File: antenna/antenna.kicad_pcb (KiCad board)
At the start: 2 copper layers, 50 x 43.3 mm, 17 parts, among them J1 Conn_01x05_Pin, J2 Conn_01x05_Pin, J3 Conn_01x05_Pin, J5 USB_C_Receptacle, U1 ESP32-C3-WROOM-02, U2 AMS1117-3.3

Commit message: great success!
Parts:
- removed JP1: SolderJumper_2_Open, Jumper:SolderJumper-2_P1.3mm_Open_RoundedPad1.0x1.5mm
- added C6: 4u7F, Capacitor_SMD:C_0805_2012Metric_Pad1.18x1.45mm_HandSolder, B.Cu at (138.8, 86.8)
- added R1: 10k, Resistor_SMD:R_0805_2012Metric_Pad1.20x1.40mm_HandSolder, B.Cu at (136.2, 86.8)
- added R2: 10k, Resistor_SMD:R_0805_2012Metric_Pad1.20x1.40mm_HandSolder, B.Cu at (138.8, 82.5)
- added SW1: SW_Push, 0_NRD_footprints:SW_PUSH-12mm_Wuerth-430456085736, B.Cu at (147.5, 64.8)
- added SW2: SW_Push, Button_Switch_SMD:SW_Tactile_SPST_NO_Straight_CK_PTS636Sx25SMTRLFS, B.Cu at (164.5, 91.0)
- C1: value C -> 4u7F
- C2: value 100nF -> 4u7F
- moved C4 10.2 mm to (133.0, 82.2), turned to 60 degrees
- moved C5 7.60 mm to (136.2, 82.5), turned to 90 degrees
- moved U2 4.51 mm to (133.2, 87.0), turned to -90 degrees
- moved C3 2.75 mm to (138.8, 91.0)
- moved C2 1.85 mm to (136.2, 91.0)
- moved D1 1.02 mm to (151.0, 86.5)
- moved U1 0.98 mm to (150.0, 86.2)
- moved C1 0.75 mm to (145.5, 86.0)
- moved J1 0.73 mm to (155.8, 91.2)
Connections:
- J2 pad 3: Net-(J2-Pin_3) -> unconnected-(J2-Pin_3-Pad3)
- U1 pad 16: unconnected-(U1-IO2-Pad16) -> Net-(D1-DIN)
- U1 pad 18: Net-(D1-DIN) -> Net-(U1-IO0)
- U1 pad 2: unconnected-(U1-EN-Pad2) -> Net-(U1-EN)
- U1 pad 7: unconnected-(U1-IO8-Pad7) -> Net-(U1-IO8)
- U1 pad 8: unconnected-(U1-IO9-Pad8) -> Net-(U1-IO9)
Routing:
- net GND: track 28.2 -> 178.2 mm, vias 5 -> 4
- net +5V: track 39.1 -> 154.0 mm, vias 10 -> 9
- net Net-(U1-IO9): track 0.00 -> 25.6 mm
- net Net-(U1-3V3): track 6.43 -> 23.3 mm, vias 0 -> 2
- net Net-(J2-Pin_3): track 10.5 -> 0.00 mm
- net Net-(D5-DOUT): track 14.1 -> 4.26 mm
- net Net-(U1-EN): track 0.00 -> 8.76 mm
- net /D-: track 9.54 -> 5.89 mm
- net Net-(U1-IO8): track 0.00 -> 3.22 mm
- net Net-(D1-DOUT): track 22.2 -> 19.7 mm
- net Net-(U1-IO0): track 0.00 -> 2.39 mm
- net Net-(D2-DOUT): track 13.9 -> 15.5 mm
- net Net-(D1-DIN): track 15.6 -> 16.5 mm, vias 0 -> 1
- net /D+: track 12.3 -> 11.6 mm
- removed copper zone on B.Cu, net +5V
- removed copper zone on F.Cu, net +5V
- removed copper zone on F.Cu, net GND

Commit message: updated all coolness
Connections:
- J2 pad 3: unconnected-(J2-Pin_3-Pad3) -> Net-(J2-Pin_3)
- SW1 pad 2: Net-(U1-IO9) -> Net-(J2-Pin_3)
- U1 pad 8: Net-(U1-IO9) -> Net-(J2-Pin_3)
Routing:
- net Net-(J2-Pin_3): track 0.00 -> 47.8 mm
- net GND: track 178.2 -> 205.3 mm, vias 4 -> 9
- net Net-(U1-IO9): track 25.6 -> 0.00 mm
- net +5V: track 154.0 -> 142.7 mm, vias 9 -> 11
- net /D-: track 5.89 -> 7.57 mm, vias 1 -> 2
- net Net-(D1-DIN): track 16.5 -> 15.9 mm
- net /D+: vias 2 -> 1

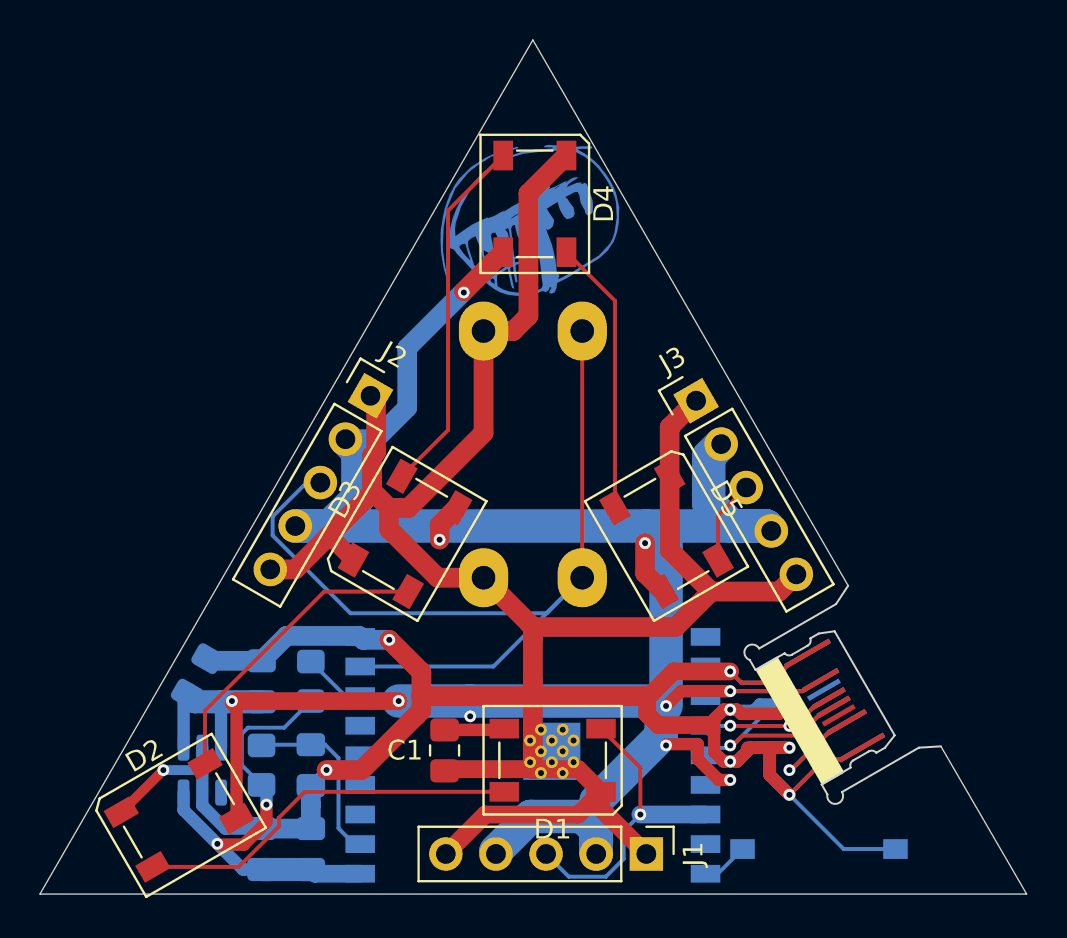
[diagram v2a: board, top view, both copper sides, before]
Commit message: added mic to antenna, decagons, octagons and all the shenanigans
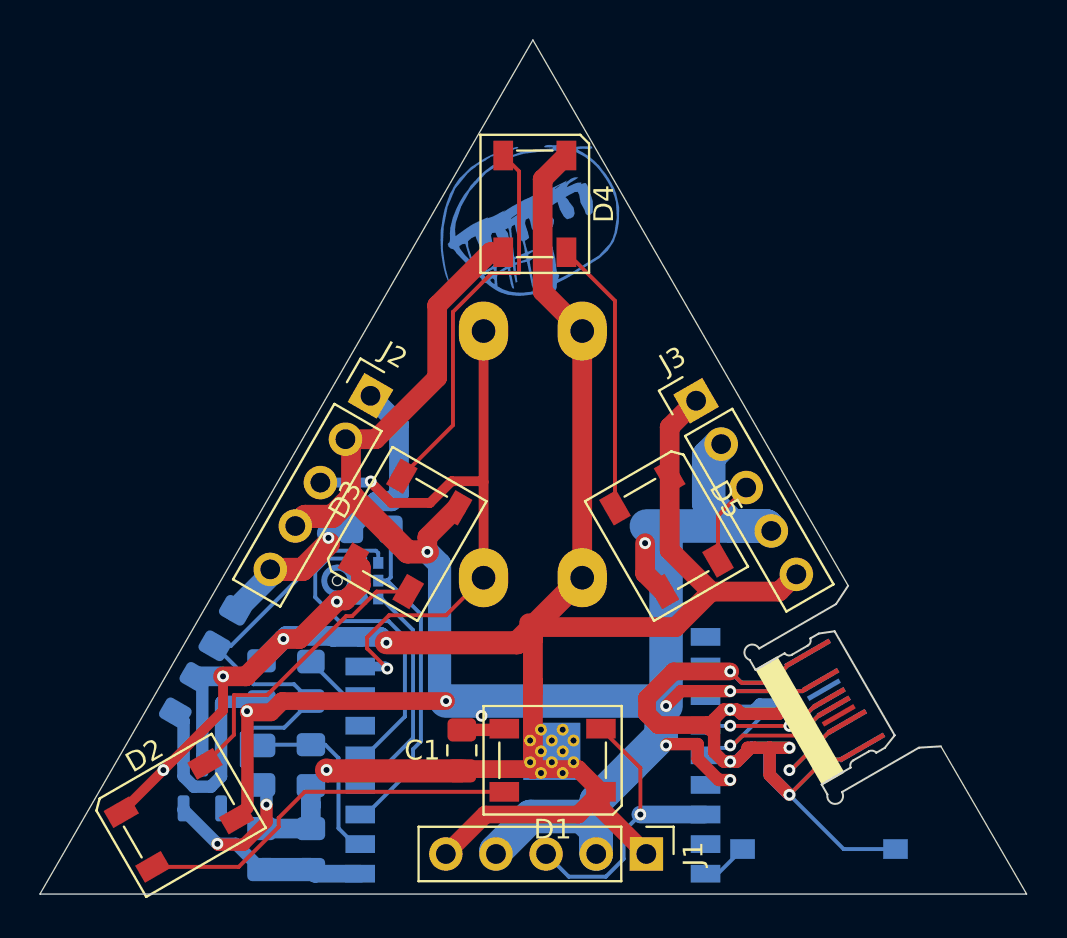
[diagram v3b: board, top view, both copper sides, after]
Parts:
- added C7: 4u7F, Capacitor_SMD:C_0805_2012Metric_Pad1.18x1.45mm_HandSolder, B.Cu at (134.4, 79.8)
- added MK1: ICS-43434, Sensor_Audio:InvenSense_ICS-43434-6_3.5x2.65mm, B.Cu at (140.8, 77.4)
- added R3: 100k, Resistor_SMD:R_0805_2012Metric_Pad1.20x1.40mm_HandSolder, B.Cu at (141.8, 74.8)
- moved SW1 13.5 mm to (152.5, 77.3), turned to 90 degrees
- moved C4 1.12 mm to (132.4, 83.2)
- moved C1 0.87 mm to (146.4, 86.0)
- moved U2 0.80 mm to (133.2, 87.8)
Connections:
- net Net-(U1-3V3) renamed +3.3V
- D1 pad 2: Net-(D1-DIN) -> GND
- J1 pad 3: Net-(D1-DIN) -> GND
- SW2 pad 1: GND -> Net-(U1-IO0)
- SW2 pad 2: Net-(U1-IO0) -> GND
- U1 pad 16: Net-(D1-DIN) -> GND
- U1 pad 3: unconnected-(U1-IO4-Pad3) -> Net-(MK1-SD)
- U1 pad 4: unconnected-(U1-IO5-Pad4) -> Net-(MK1-WS)
- U1 pad 5: unconnected-(U1-IO6-Pad5) -> Net-(MK1-SCK)
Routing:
- net Net-(MK1-SD): track 0.00 -> 17.6 mm
- net Net-(MK1-SCK): track 0.00 -> 16.5 mm
- net +3.3V: track 23.3 -> 39.4 mm
- net Net-(D1-DIN): track 15.9 -> 0.00 mm, vias 1 -> 0
- net GND: track 205.3 -> 218.2 mm, vias 9 -> 14
- net Net-(MK1-WS): track 0.00 -> 11.6 mm
- net +5V: track 142.7 -> 139.4 mm, vias 11 -> 10
- net Net-(J2-Pin_3): track 47.8 -> 44.8 mm, vias 0 -> 2
- net Net-(D3-DOUT): track 18.4 -> 19.8 mm

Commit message: url-update and some bla
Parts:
- removed C7: 4u7F, Capacitor_SMD:C_0805_2012Metric_Pad1.18x1.45mm_HandSolder
- removed MK1: ICS-43434, Sensor_Audio:InvenSense_ICS-43434-6_3.5x2.65mm
- removed R3: 100k, Resistor_SMD:R_0805_2012Metric_Pad1.20x1.40mm_HandSolder
- moved SW1 13.5 mm to (147.5, 64.8), turned to -90 degrees
- moved C4 1.12 mm to (133.0, 82.2)
- moved C1 0.87 mm to (145.5, 86.0)
- moved U2 0.80 mm to (133.2, 87.0)
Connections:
- net +3.3V renamed Net-(U1-3V3)
- D1 pad 2: GND -> Net-(D1-DIN)
- J1 pad 3: GND -> Net-(D1-DIN)
- SW2 pad 1: Net-(U1-IO0) -> GND
- SW2 pad 2: GND -> Net-(U1-IO0)
- U1 pad 16: GND -> Net-(D1-DIN)
- U1 pad 3: Net-(MK1-SD) -> unconnected-(U1-IO4-Pad3)
- U1 pad 4: Net-(MK1-WS) -> unconnected-(U1-IO5-Pad4)
- U1 pad 5: Net-(MK1-SCK) -> unconnected-(U1-IO6-Pad5)
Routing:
- net Net-(MK1-SD): track 17.6 -> 0.00 mm
- net Net-(MK1-SCK): track 16.5 -> 0.00 mm
- net Net-(U1-3V3): track 39.4 -> 23.3 mm
- net Net-(D1-DIN): track 0.00 -> 15.9 mm, vias 0 -> 1
- net GND: track 218.2 -> 205.3 mm, vias 14 -> 9
- net Net-(MK1-WS): track 11.6 -> 0.00 mm
- net +5V: track 139.4 -> 142.7 mm, vias 10 -> 11
- net Net-(J2-Pin_3): track 44.8 -> 47.8 mm, vias 2 -> 0
- net Net-(D3-DOUT): track 19.8 -> 18.4 mm
